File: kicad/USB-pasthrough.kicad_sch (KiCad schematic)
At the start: 93 parts, among them J1 USB_Power, J10 MicroSD, J4 Power_Sel, J5 SPI Display, J6 SWD, J7 Cortex Debug, J8 USB_C, J9 USB_A, SW1 Boot0, SW2 Reset, U1 STM32F723VET6, U2 AMS1117, Y1 8 MHz

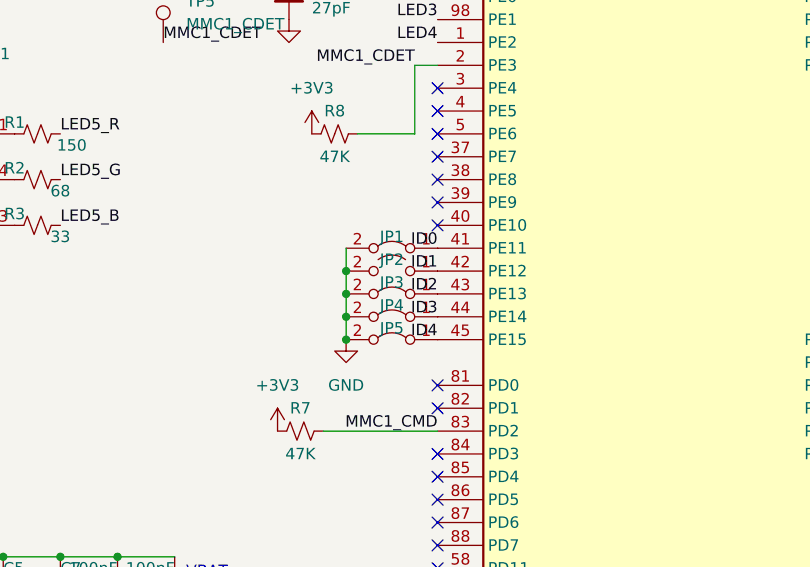
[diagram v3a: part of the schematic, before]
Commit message: Rework ID jumper labeling
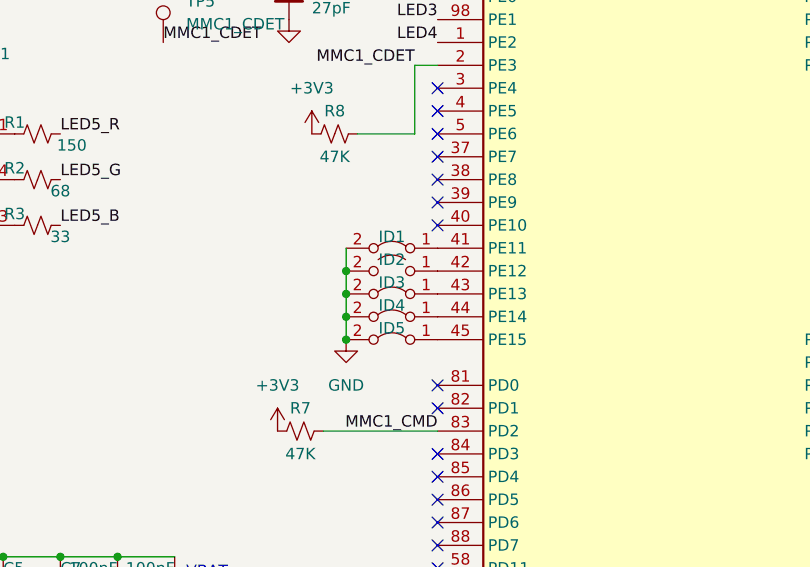
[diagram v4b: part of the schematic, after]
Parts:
- renumbered JP1 to ID1, JP2 to ID2, JP3 to ID3, JP4 to ID4, JP5 to ID5
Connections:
- net ID0: no longer names the net of ID1.1 (A), U1.41 (PE11)
- net ID1: no longer names the net of ID2.1 (A), U1.42 (PE12)
- net ID2: no longer names the net of ID3.1 (A), U1.43 (PE13)
- net ID3: no longer names the net of ID4.1 (A), U1.44 (PE14)
- net ID4: no longer names the net of ID5.1 (A), U1.45 (PE15)
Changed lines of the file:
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@@
     (effects (font (size 1.27 1.27)) (justify left bottom))
   )
-  (label "ID0" (at 81.28 119.38 180)
-    (effects (font (size 1.27 1.27)) (justify right bottom))
-  )
   (label "VBUS_PWR" (at 50.8 27.94 0)
     (effects (font (size 1.27 1.27)) (justify left bottom))
@@
     (effects (font (size 1.27 1.27)) (justify right bottom))
   )
-  (label "ID4" (at 81.28 129.54 180)
-    (effects (font (size 1.27 1.27)) (justify right bottom))
-  )
   (label "USBA+" (at 243.84 107.95 0)
     (effects (font (size 1.27 1.27)) (justify left bottom))
@@
     (effects (font (size 1.27 1.27)) (justify left bottom))
   )
-  (label "ID2" (at 81.28 124.46 180)
-    (effects (font (size 1.27 1.27)) (justify right bottom))
-  )
   (label "LCD_CS" (at 181.61 118.11 180)
     (effects (font (size 1.27 1.27)) (justify right bottom))
@@
     (effects (font (size 1.27 1.27)) (justify right bottom))
   )
-  (label "ID1" (at 81.28 121.92 180)
-    (effects (font (size 1.27 1.27)) (justify right bottom))
-  )
-  (label "ID3" (at 81.28 127 180)
-    (effects (font (size 1.27 1.27)) (justify right bottom))
-  )
   (label "PA13" (at 132.08 93.98 0)
     (effects (font (size 1.27 1.27)) (justify left bottom))
@@
   (symbol (lib_id "Jumper:Jumper_2_Open") (at 76.2 121.92 0) (mirror y) (unit 1)
     (in_bom yes) (on_board yes)
-    (property "Reference" "JP2" (id 0) (at 76.2 120.65 0))
+    (property "Reference" "ID2" (id 0) (at 76.2 120.65 0))
     (property "Value" "Jumper_2_Bridged" (id 1) (at 76.2 118.11 0)
       (effects (font (size 1.27 1.27)) hide)
@@
   (symbol (lib_id "Jumper:Jumper_2_Bridged") (at 76.2 119.38 0) (mirror y) (unit 1)
     (in_bom yes) (on_board yes)
-    (property "Reference" "JP1" (id 0) (at 76.2 118.11 0))
+    (property "Reference" "ID1" (id 0) (at 76.2 118.11 0))
     (property "Value" "Jumper_2_Bridged" (id 1) (at 76.2 115.57 0)
       (effects (font (size 1.27 1.27)) hide)
@@
   (symbol (lib_id "Jumper:Jumper_2_Bridged") (at 76.2 127 0) (mirror y) (unit 1)
     (in_bom yes) (on_board yes)
-    (property "Reference" "JP4" (id 0) (at 76.2 125.73 0))
+    (property "Reference" "ID4" (id 0) (at 76.2 125.73 0))
     (property "Value" "Jumper_2_Bridged" (id 1) (at 76.2 123.19 0)
       (effects (font (size 1.27 1.27)) hide)
@@
   (symbol (lib_id "Jumper:Jumper_2_Bridged") (at 76.2 124.46 0) (mirror y) (unit 1)
     (in_bom yes) (on_board yes)
-    (property "Reference" "JP3" (id 0) (at 76.2 123.19 0))
+    (property "Reference" "ID3" (id 0) (at 76.2 123.19 0))
     (property "Value" "Jumper_2_Bridged" (id 1) (at 76.2 120.65 0)
       (effects (font (size 1.27 1.27)) hide)
@@
   (symbol (lib_id "Jumper:Jumper_2_Bridged") (at 76.2 129.54 0) (mirror y) (unit 1)
     (in_bom yes) (on_board yes)
-    (property "Reference" "JP5" (id 0) (at 76.2 128.27 0))
+    (property "Reference" "ID5" (id 0) (at 76.2 128.27 0))
     (property "Value" "Jumper_2_Bridged" (id 1) (at 76.2 125.73 0)
       (effects (font (size 1.27 1.27)) hide)
@@
       (reference "H4") (unit 1) (value "MountingHole") (footprint "MountingHole:MountingHole_2.2mm_M2_Pad")
     )
+    (path "/1858f103-0550-4454-a9a8-cb3c44998e1e"
+      (reference "ID1") (unit 1) (value "Jumper_2_Bridged") (footprint "Jumper:SolderJumper-2_P1.3mm_Bridged_Pad1.0x1.5mm")
+    )
+    (path "/1586b523-a3cf-43e8-bf9d-0533c598fcc1"
+      (reference "ID2") (unit 1) (value "Jumper_2_Bridged") (footprint "Jumper:SolderJumper-2_P1.3mm_Open_Pad1.0x1.5mm")
+    )
+    (path "/8d554622-7ff9-41d4-a107-16b60e1fce82"
+      (reference "ID3") (unit 1) (value "Jumper_2_Bridged") (footprint "Jumper:SolderJumper-2_P1.3mm_Bridged_Pad1.0x1.5mm")
+    )
+    (path "/8b9373f4-2597-4d9f-8245-62eb92cb212f"
+      (reference "ID4") (unit 1) (value "Jumper_2_Bridged") (footprint "Jumper:SolderJumper-2_P1.3mm_Bridged_Pad1.0x1.5mm")
+    )
+    (path "/95c1312c-0851-4fe5-a936-d7533c7cbaf8"
+      (reference "ID5") (unit 1) (value "Jumper_2_Bridged") (footprint "Jumper:SolderJumper-2_P1.3mm_Bridged_Pad1.0x1.5mm")
+    )
     (path "/7cf7e8fc-d4c5-4161-b905-d74139026239"
       (reference "J1") (unit 1) (value "USB_Power") (footprint "Connector_USB:USB_C_Receptacle_GCT_USB4135-GF-A_6P_TopMnt_Horizontal")
@@
       (reference "J10") (unit 1) (value "MicroSD") (footprint "Connector_Card:microSD_HC_Hirose_DM3AT-SF-PEJM5")
     )
-    (path "/1858f103-0550-4454-a9a8-cb3c44998e1e"
-      (reference "JP1") (unit 1) (value "Jumper_2_Bridged") (footprint "Jumper:SolderJumper-2_P1.3mm_Bridged_Pad1.0x1.5mm")
-    )
-    (path "/1586b523-a3cf-43e8-bf9d-0533c598fcc1"
-      (reference "JP2") (unit 1) (value "Jumper_2_Bridged") (footprint "Jumper:SolderJumper-2_P1.3mm_Open_Pad1.0x1.5mm")
-    )
-    (path "/8d554622-7ff9-41d4-a107-16b60e1fce82"
-      (reference "JP3") (unit 1) (value "Jumper_2_Bridged") (footprint "Jumper:SolderJumper-2_P1.3mm_Bridged_Pad1.0x1.5mm")
-    )
-    (path "/8b9373f4-2597-4d9f-8245-62eb92cb212f"
-      (reference "JP4") (unit 1) (value "Jumper_2_Bridged") (footprint "Jumper:SolderJumper-2_P1.3mm_Bridged_Pad1.0x1.5mm")
-    )
-    (path "/95c1312c-0851-4fe5-a936-d7533c7cbaf8"
-      (reference "JP5") (unit 1) (value "Jumper_2_Bridged") (footprint "Jumper:SolderJumper-2_P1.3mm_Bridged_Pad1.0x1.5mm")
-    )
     (path "/97339053-1ba0-429b-8e6a-4e4aa25ddc74"

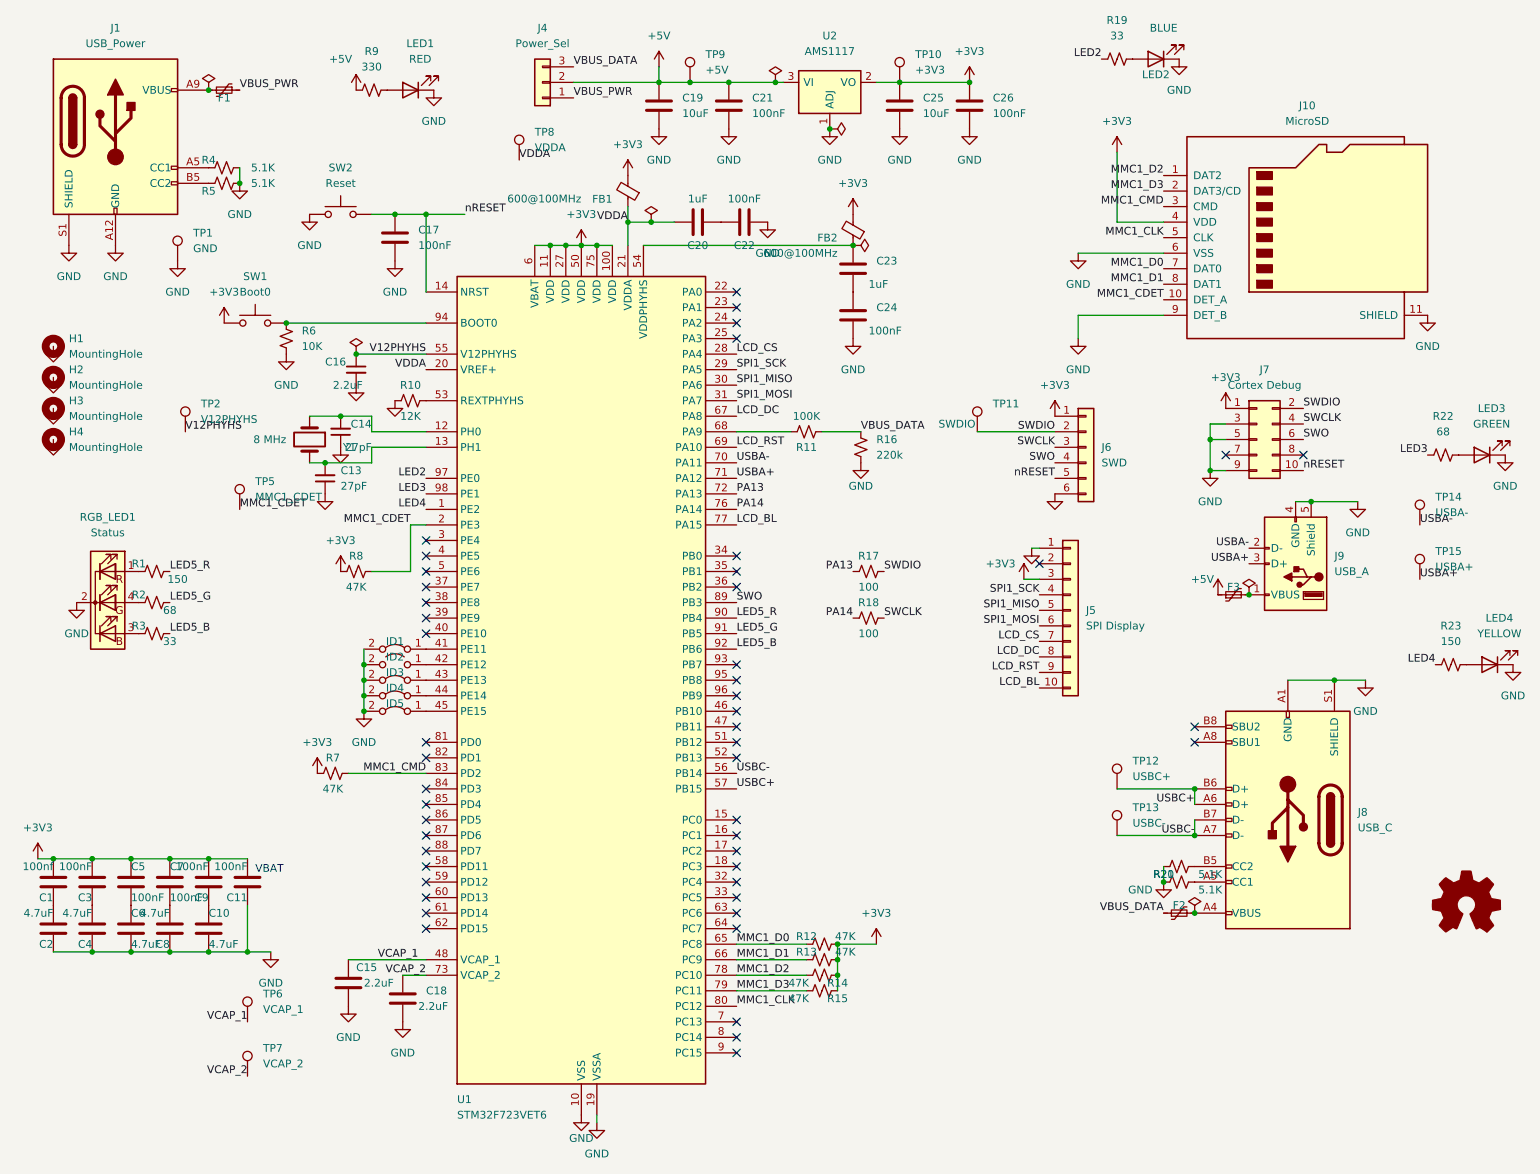
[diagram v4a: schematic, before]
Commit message: Reannotate based on position on PCB
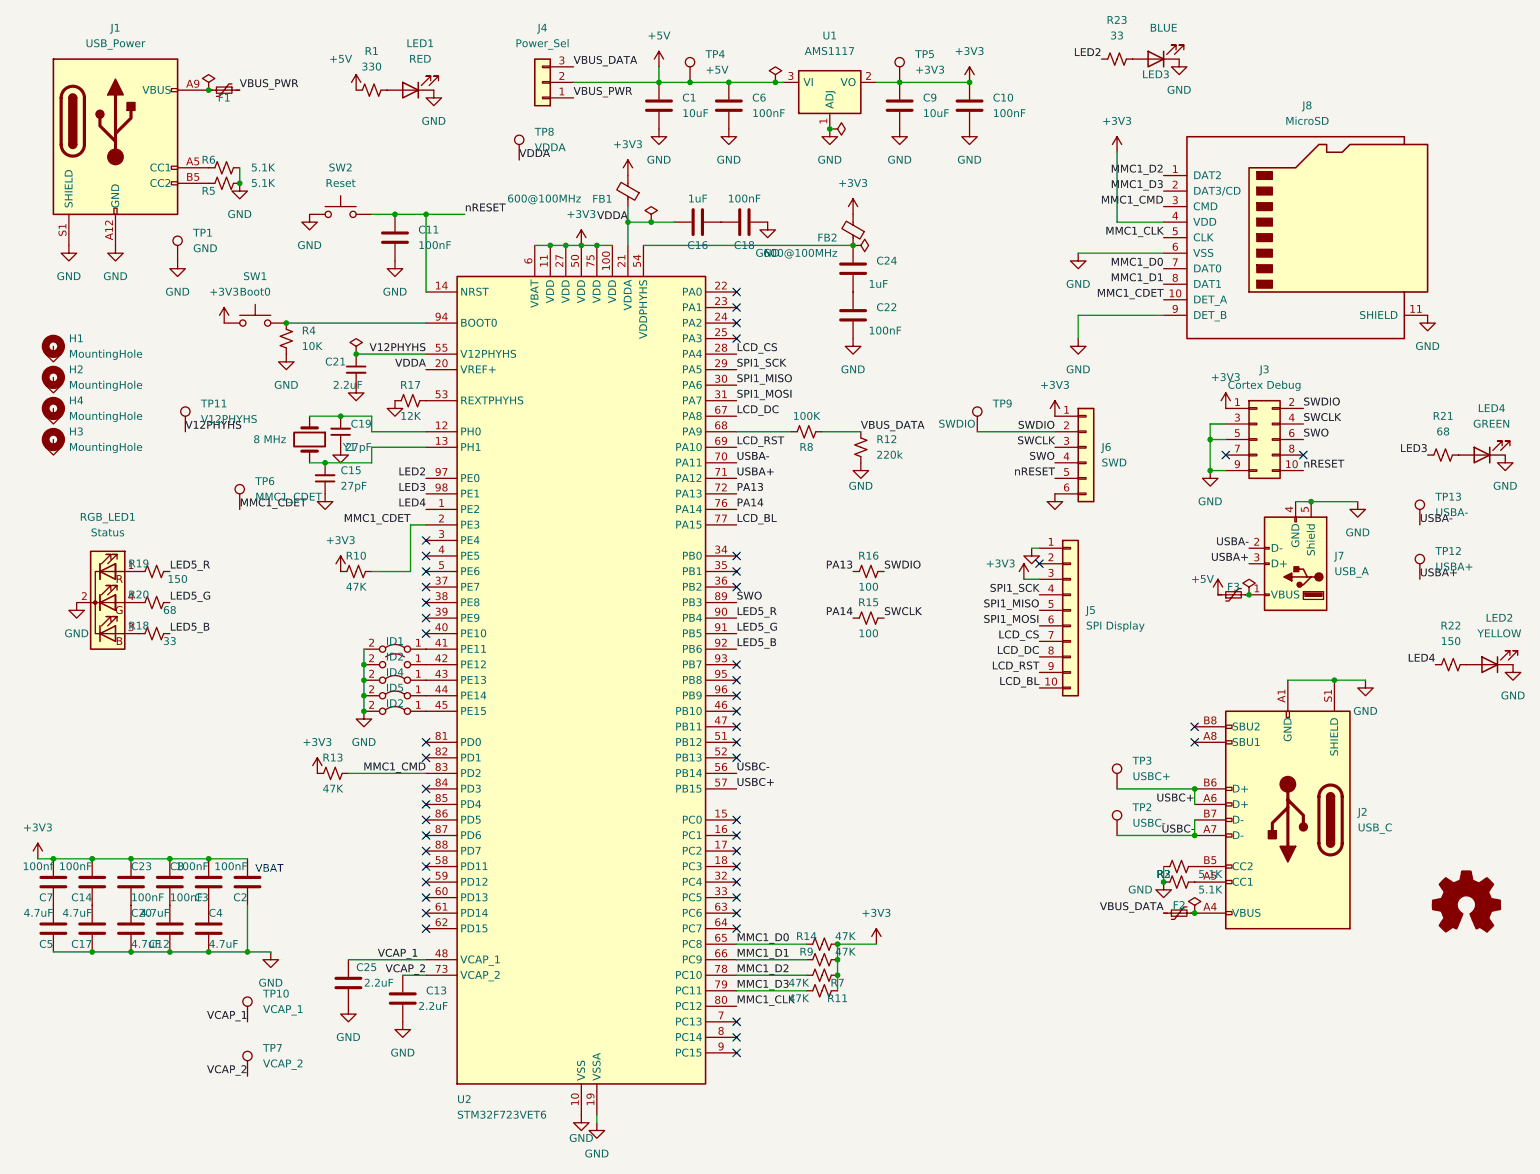
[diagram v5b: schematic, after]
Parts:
- renumbered C19 to C1, C26 to C10, C17 to C11, C8 to C12, C18 to C13, C3 to C14, C13 to C15, C20 to C16, C4 to C17, C22 to C18, C14 to C19, C11 to C2, C6 to C20, C16 to C21, C24 to C22, C5 to C23, C23 to C24, C15 to C25, C9 to C3, C10 to C4, C2 to C5, C21 to C6, C1 to C7, C7 to C8, C25 to C9, H4 to H3, H3 to H4, ID5 to ID2, ID3 to ID4, ID4 to ID5, J8 to J2, J7 to J3, J9 to J7, J10 to J8, LED4 to LED2, LED2 to LED3, LED3 to LED4, R9 to R1, R8 to R10, R15 to R11, R16 to R12, R7 to R13, R12 to R14, R18 to R15, R17 to R16, R10 to R17, R3 to R18, R1 to R19, R20 to R2, R2 to R20, R22 to R21, R23 to R22, R19 to R23, R21 to R3, R6 to R4, R4 to R6, R14 to R7, R11 to R8, R13 to R9, TP6 to TP10, TP2 to TP11, TP15 to TP12, TP14 to TP13, TP13 to TP2, TP12 to TP3, TP9 to TP4, TP10 to TP5, TP5 to TP6, TP11 to TP9, U2 to U1, U1 to U2

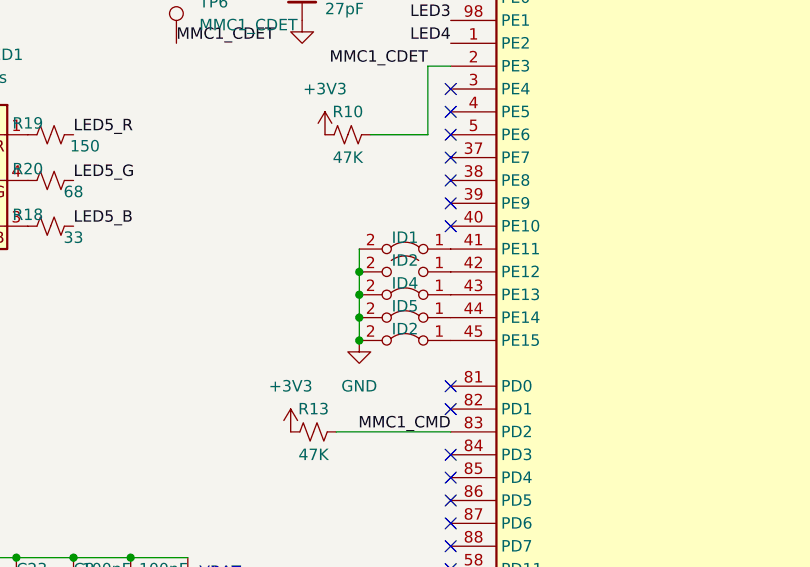
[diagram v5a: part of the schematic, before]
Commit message: Fix ID jumper references
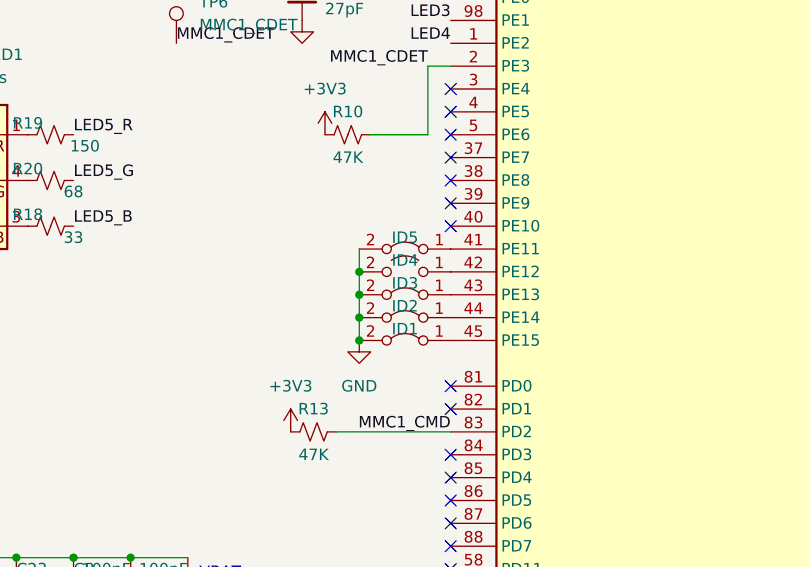
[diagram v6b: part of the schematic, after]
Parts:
- renumbered ID2 to ID1, ID5 to ID2, ID4 to ID3, ID2 to ID4, ID1 to ID5
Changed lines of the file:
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@@
   (symbol (lib_id "Jumper:Jumper_2_Open") (at 76.2 121.92 0) (mirror y) (unit 1)
     (in_bom yes) (on_board yes)
-    (property "Reference" "ID2" (id 0) (at 76.2 120.65 0))
+    (property "Reference" "ID4" (id 0) (at 76.2 120.65 0))
     (property "Value" "Jumper_2_Bridged" (id 1) (at 76.2 118.11 0)
       (effects (font (size 1.27 1.27)) hide)
@@
   (symbol (lib_id "Jumper:Jumper_2_Bridged") (at 76.2 119.38 0) (mirror y) (unit 1)
     (in_bom yes) (on_board yes)
-    (property "Reference" "ID1" (id 0) (at 76.2 118.11 0))
+    (property "Reference" "ID5" (id 0) (at 76.2 118.11 0))
     (property "Value" "Jumper_2_Bridged" (id 1) (at 76.2 115.57 0)
       (effects (font (size 1.27 1.27)) hide)
@@
   (symbol (lib_id "Jumper:Jumper_2_Bridged") (at 76.2 127 0) (mirror y) (unit 1)
     (in_bom yes) (on_board yes)
-    (property "Reference" "ID5" (id 0) (at 76.2 125.73 0))
+    (property "Reference" "ID2" (id 0) (at 76.2 125.73 0))
     (property "Value" "Jumper_2_Bridged" (id 1) (at 76.2 123.19 0)
       (effects (font (size 1.27 1.27)) hide)
@@
   (symbol (lib_id "Jumper:Jumper_2_Bridged") (at 76.2 124.46 0) (mirror y) (unit 1)
     (in_bom yes) (on_board yes)
-    (property "Reference" "ID4" (id 0) (at 76.2 123.19 0))
+    (property "Reference" "ID3" (id 0) (at 76.2 123.19 0))
     (property "Value" "Jumper_2_Bridged" (id 1) (at 76.2 120.65 0)
       (effects (font (size 1.27 1.27)) hide)
@@
   (symbol (lib_id "Jumper:Jumper_2_Bridged") (at 76.2 129.54 0) (mirror y) (unit 1)
     (in_bom yes) (on_board yes)
-    (property "Reference" "ID2" (id 0) (at 76.2 128.27 0))
+    (property "Reference" "ID1" (id 0) (at 76.2 128.27 0))
     (property "Value" "Jumper_2_Bridged" (id 1) (at 76.2 125.73 0)
       (effects (font (size 1.27 1.27)) hide)
@@
       (reference "H4") (unit 1) (value "MountingHole") (footprint "MountingHole:MountingHole_2.2mm_M2_Pad")
     )
+    (path "/95c1312c-0851-4fe5-a936-d7533c7cbaf8"
+      (reference "ID1") (unit 1) (value "Jumper_2_Bridged") (footprint "Jumper:SolderJumper-2_P1.3mm_Bridged_Pad1.0x1.5mm")
+    )
+    (path "/8b9373f4-2597-4d9f-8245-62eb92cb212f"
+      (reference "ID2") (unit 1) (value "Jumper_2_Bridged") (footprint "Jumper:SolderJumper-2_P1.3mm_Bridged_Pad1.0x1.5mm")
+    )
+    (path "/8d554622-7ff9-41d4-a107-16b60e1fce82"
+      (reference "ID3") (unit 1) (value "Jumper_2_Bridged") (footprint "Jumper:SolderJumper-2_P1.3mm_Bridged_Pad1.0x1.5mm")
+    )
+    (path "/1586b523-a3cf-43e8-bf9d-0533c598fcc1"
+      (reference "ID4") (unit 1) (value "Jumper_2_Bridged") (footprint "Jumper:SolderJumper-2_P1.3mm_Open_Pad1.0x1.5mm")
+    )
     (path "/1858f103-0550-4454-a9a8-cb3c44998e1e"
-      (reference "ID1") (unit 1) (value "Jumper_2_Bridged") (footprint "Jumper:SolderJumper-2_P1.3mm_Bridged_Pad1.0x1.5mm")
-    )
-    (path "/1586b523-a3cf-43e8-bf9d-0533c598fcc1"
-      (reference "ID2") (unit 1) (value "Jumper_2_Bridged") (footprint "Jumper:SolderJumper-2_P1.3mm_Open_Pad1.0x1.5mm")
-    )
-    (path "/95c1312c-0851-4fe5-a936-d7533c7cbaf8"
-      (reference "ID2") (unit 1) (value "Jumper_2_Bridged") (footprint "Jumper:SolderJumper-2_P1.3mm_Bridged_Pad1.0x1.5mm")
-    )
-    (path "/8d554622-7ff9-41d4-a107-16b60e1fce82"
-      (reference "ID4") (unit 1) (value "Jumper_2_Bridged") (footprint "Jumper:SolderJumper-2_P1.3mm_Bridged_Pad1.0x1.5mm")
-    )
-    (path "/8b9373f4-2597-4d9f-8245-62eb92cb212f"
       (reference "ID5") (unit 1) (value "Jumper_2_Bridged") (footprint "Jumper:SolderJumper-2_P1.3mm_Bridged_Pad1.0x1.5mm")
     )
